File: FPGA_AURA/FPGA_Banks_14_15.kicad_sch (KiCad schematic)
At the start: 15 parts, among them U1 XC7A35T-2FTG256C

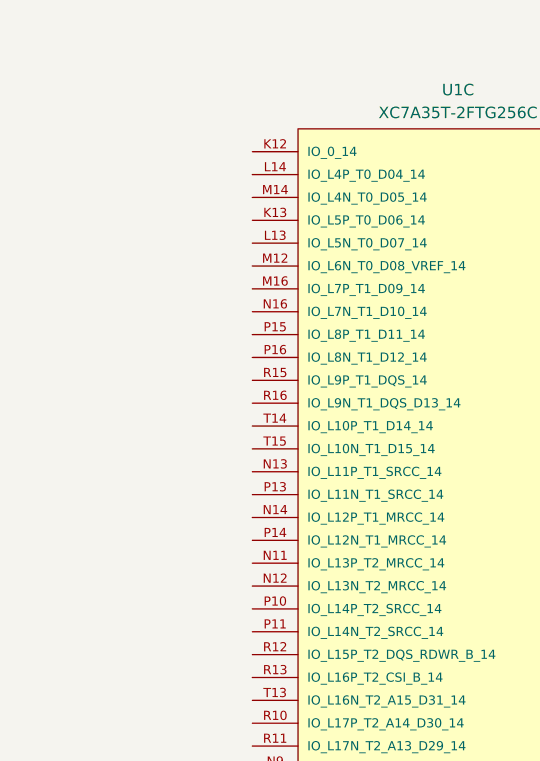
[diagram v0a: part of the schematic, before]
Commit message: Started DDR routing with new layout.
All impedances setup for PCBway 8 layer stack-up.  Routing issues with the DQ lanes still to be resolved.
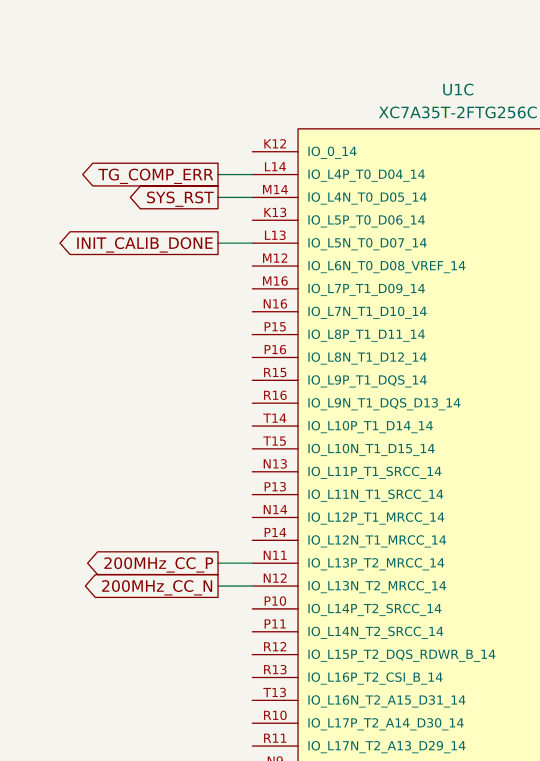
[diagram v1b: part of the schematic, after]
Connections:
- net INIT_CALIB_DONE: now reaches U1.L13 (IO_L5N_T0_D07_14)
- net TG_COMP_ERR: now reaches U1.L14 (IO_L4P_T0_D04_14)
- net SYS_RST: now reaches U1.M14 (IO_L4N_T0_D05_14)
- net 200MHz_CC_P: now reaches U1.N11 (IO_L13P_T2_MRCC_14)
- net 200MHz_CC_N: now reaches U1.N12 (IO_L13N_T2_MRCC_14)
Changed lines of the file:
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@@
+	(wire
+		(pts
+			(xy 72.39 73.66) (xy 68.58 73.66)
+		)
+		(stroke
+			(width 0)
+			(type default)
+		)
+	)
 	(wire
 		(pts
@@
 	(wire
 		(pts
+			(xy 72.39 119.38) (xy 68.58 119.38)
+		)
+		(stroke
+			(width 0)
+			(type default)
+		)
+	)
+	(wire
+		(pts
 			(xy 113.03 29.21) (xy 113.03 30.48)
 		)
@@
 	(wire
 		(pts
+			(xy 72.39 81.28) (xy 68.58 81.28)
+		)
+		(stroke
+			(width 0)
+			(type default)
+		)
+	)
+	(wire
+		(pts
 			(xy 220.98 29.21) (xy 224.79 29.21)
 		)
@@
 	(wire
 		(pts
+			(xy 72.39 116.84) (xy 68.58 116.84)
+		)
+		(stroke
+			(width 0)
+			(type default)
+		)
+	)
+	(wire
+		(pts
 			(xy 143.51 92.71) (xy 143.51 93.98)
 		)
@@
 	(wire
 		(pts
+			(xy 72.39 76.2) (xy 68.58 76.2)
+		)
+		(stroke
+			(width 0)
+			(type default)
+		)
+	)
+	(wire
+		(pts
 			(xy 220.98 87.63) (xy 224.79 87.63)
 		)
@@
 		)
 	)
+	(global_label "TG_COMP_ERR"
+		(shape output)
+		(at 68.58 73.66 180)
+		(fields_autoplaced yes)
+		(effects
+			(font
+				(size 1.27 1.27)
+			)
+			(justify right)
+		)
+		(property "Intersheetrefs" "${INTERSHEET_REFS}"
+			(at 52.4111 73.66 0)
+			(hide yes)
+			(show_name no)
+			(do_not_autoplace no)
+			(effects
+				(font
+					(size 1.27 1.27)
+				)
+				(justify right)
+			)
+		)
+	)
 	(global_label "DDR3_CKE"
 		(shape output)
@@
 		)
 	)
+	(global_label "200MHz_CC_N"
+		(shape output)
+		(at 68.58 119.38 180)
+		(fields_autoplaced yes)
+		(effects
+			(font
+				(size 1.27 1.27)
+			)
+			(justify right)
+		)
+		(property "Intersheetrefs" "${INTERSHEET_REFS}"
+			(at 52.3506 119.38 0)
+			(hide yes)
+			(show_name no)
+			(do_not_autoplace no)
+			(effects
+				(font
+					(size 1.27 1.27)
+				)
+				(justify right)
+			)
+		)
+	)
 	(global_label "DDR3_DQS0+"
 		(shape output)
@@
 		)
 	)
+	(global_label "INIT_CALIB_DONE"
+		(shape output)
+		(at 68.58 81.28 180)
+		(fields_autoplaced yes)
+		(effects
+			(font
+				(size 1.27 1.27)
+			)
+			(justify right)
+		)
+		(property "Intersheetrefs" "${INTERSHEET_REFS}"
+			(at 49.8104 81.28 0)
+			(hide yes)
+			(show_name no)
+			(do_not_autoplace no)
+			(effects
+				(font
+					(size 1.27 1.27)
+				)
+				(justify right)
+			)
+		)
+	)
 	(global_label "DDR3_CAS"
 		(shape output)
@@
 		)
 	)
+	(global_label "200MHz_CC_P"
+		(shape output)
+		(at 68.58 116.84 180)
+		(fields_autoplaced yes)
+		(effects
+			(font
+				(size 1.27 1.27)
+			)
+			(justify right)
+		)
+		(property "Intersheetrefs" "${INTERSHEET_REFS}"
+			(at 52.4111 116.84 0)
+			(hide yes)
+			(show_name no)
+			(do_not_autoplace no)
+			(effects
+				(font
+					(size 1.27 1.27)
+				)
+				(justify right)
+			)
+		)
+	)
 	(global_label "DDR3_RESET"
 		(shape output)
@@
 			)
 		)
+	)
+	(global_label "SYS_RST"
+		(shape output)
+		(at 68.58 76.2 180)
+		(fields_autoplaced yes)
+		(effects
+			(font
+				(size 1.27 1.27)
+			)
+			(justify right)
+		)
+		(property "Intersheetrefs" "${INTERSHEET_REFS}"
+			(at 57.6725 76.2 0)
+			(hide yes)
+			(show_name no)
+			(do_not_autoplace no)
+			(effects
+				(font
+					(size 1.27 1.27)
+				)
+				(justify right)
+			)
+		)

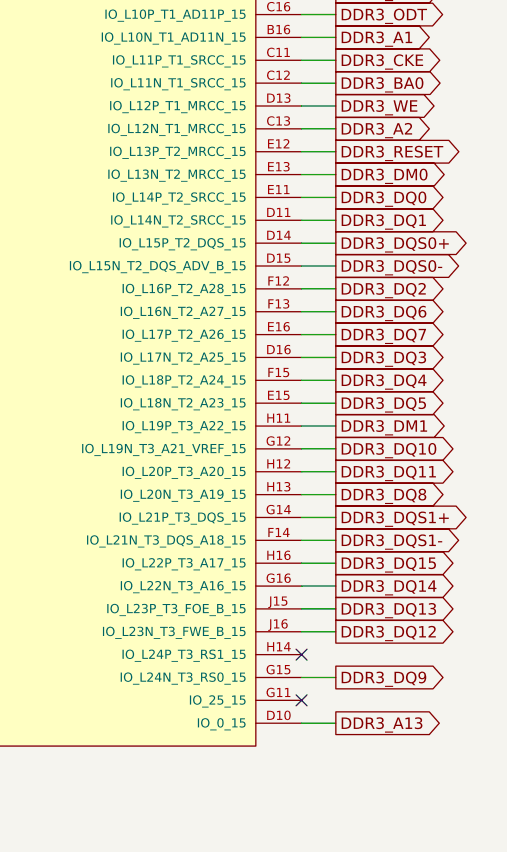
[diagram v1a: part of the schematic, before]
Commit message: DDR3 Routing complete on 3 layers, top layer left.
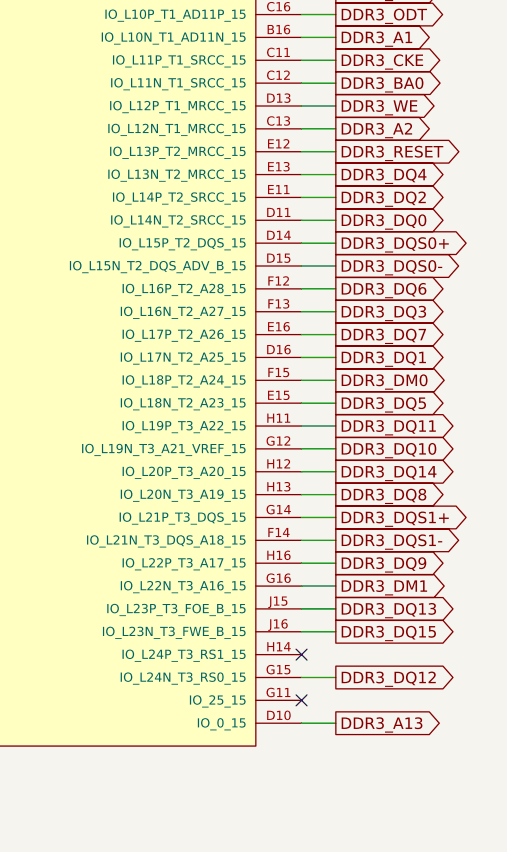
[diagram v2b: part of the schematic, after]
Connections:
- net DDR3_DM0: now also U1.F15 (IO_L18P_T2_A24_15); no longer U1.E13 (IO_L13N_T2_MRCC_15)
- net DDR3_DM1: now also U1.G16 (IO_L22N_T3_A16_15); no longer U1.H11 (IO_L19P_T3_A22_15)
- net DDR3_DQ0: now also U1.D11 (IO_L14N_T2_SRCC_15); no longer U1.E11 (IO_L14P_T2_SRCC_15)
- net DDR3_DQ1: now also U1.D16 (IO_L17N_T2_A25_15); no longer U1.D11 (IO_L14N_T2_SRCC_15)
- net DDR3_DQ11: now also U1.H11 (IO_L19P_T3_A22_15); no longer U1.H12 (IO_L20P_T3_A20_15)
- net DDR3_DQ12: now also U1.G15 (IO_L24N_T3_RS0_15); no longer U1.J16 (IO_L23N_T3_FWE_B_15)
- net DDR3_DQ14: now also U1.H12 (IO_L20P_T3_A20_15); no longer U1.G16 (IO_L22N_T3_A16_15)
- net DDR3_DQ15: now also U1.J16 (IO_L23N_T3_FWE_B_15); no longer U1.H16 (IO_L22P_T3_A17_15)
- net DDR3_DQ2: now also U1.E11 (IO_L14P_T2_SRCC_15); no longer U1.F12 (IO_L16P_T2_A28_15)
- net DDR3_DQ3: now also U1.F13 (IO_L16N_T2_A27_15); no longer U1.D16 (IO_L17N_T2_A25_15)
- net DDR3_DQ4: now also U1.E13 (IO_L13N_T2_MRCC_15); no longer U1.F15 (IO_L18P_T2_A24_15)
- net DDR3_DQ6: now also U1.F12 (IO_L16P_T2_A28_15); no longer U1.F13 (IO_L16N_T2_A27_15)
- net DDR3_DQ9: now also U1.H16 (IO_L22P_T3_A17_15); no longer U1.G15 (IO_L24N_T3_RS0_15)
